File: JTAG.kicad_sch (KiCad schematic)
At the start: 7 parts, among them J2 JTAG_HEADER, J3 JTAG_HEADER

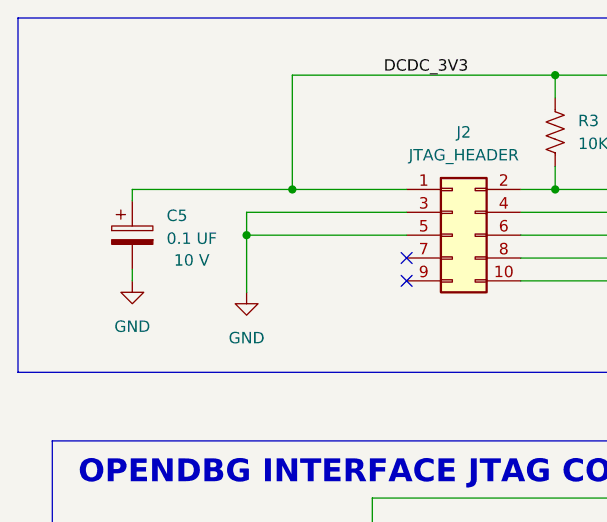
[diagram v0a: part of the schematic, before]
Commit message: menambah lebih dari setengah footprint
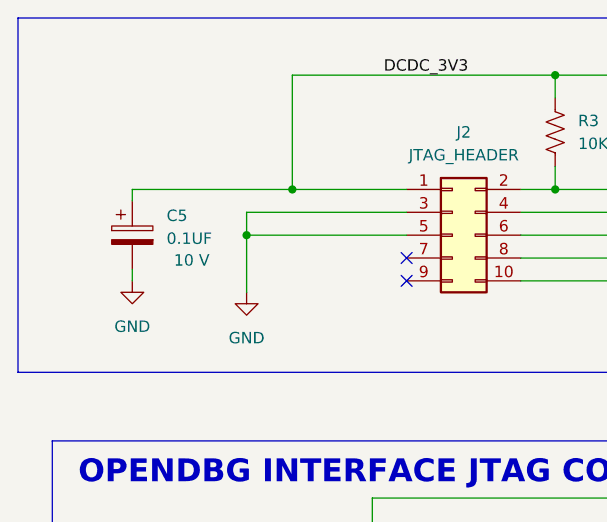
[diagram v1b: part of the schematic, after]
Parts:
- C33: footprint (none) -> Capacitor_SMD:C_0402_1005Metric; MANUFACTURER (none) -> CC0402KRX5R6BB104
- C5: value 0.1 UF -> 0.1UF; footprint (none) -> Capacitor_SMD:C_0402_1005Metric; MANUFACTURER (none) -> CC0402KRX5R6BB104
- R24, R3, R4: footprint (none) -> Resistor_SMD:R_0402_1005Metric
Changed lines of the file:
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@@
 			)
 		)
-		(property "Footprint" ""
+		(property "Footprint" "Resistor_SMD:R_0402_1005Metric"
 			(at 111.506 32.004 90)
 			(effects
@@
 			)
 		)
+		(property "DigikeyPartNumber" ""
+			(at 110.49 31.75 0)
+			(effects
+				(font
+					(size 1.27 1.27)
+				)
+				(hide yes)
+			)
+		)
 		(pin "1"
 		)
@@
 			)
 		)
-		(property "Value" "0.1 UF"
+		(property "Value" "0.1UF"
 			(at 67.31 43.5609 0)
 			(effects
@@
 			)
 		)
-		(property "Footprint" ""
+		(property "Footprint" "Capacitor_SMD:C_0402_1005Metric"
 			(at 64.4652 46.99 0)
 			(effects
@@
 					(size 1.27 1.27)
 				)
+			)
+		)
+		(property "DigikeyPartNumber" ""
+			(at 63.5 43.18 0)
+			(effects
+				(font
+					(size 1.27 1.27)
+				)
+				(hide yes)
+			)
+		)
+		(property "MANUFACTURER" "CC0402KRX5R6BB104"
+			(at 63.5 43.18 0)
+			(effects
+				(font
+					(size 1.27 1.27)
+				)
+				(hide yes)
 			)
 		)
@@
 			)
 		)
+		(property "DigikeyPartNumber" ""
+			(at 99.06 43.18 0)
+			(effects
+				(font
+					(size 1.27 1.27)
+				)
+				(hide yes)
+			)
+		)
 		(pin "8"
 		)
@@
 			)
 		)
-		(property "Footprint" ""
+		(property "Footprint" "Resistor_SMD:R_0402_1005Metric"
 			(at 120.396 32.004 90)
 			(effects
@@
 		)
 		(property "Description" "Resistor, US symbol"
+			(at 119.38 31.75 0)
+			(effects
+				(font
+					(size 1.27 1.27)
+				)
+				(hide yes)
+			)
+		)
+		(property "DigikeyPartNumber" ""
 			(at 119.38 31.75 0)
 			(effects
@@
 			)
 		)
-		(property "Footprint" ""
+		(property "Footprint" "Capacitor_SMD:C_0402_1005Metric"
 			(at 74.93 88.9 0)
 			(effects
@@
 					(size 1.27 1.27)
 				)
+			)
+		)
+		(property "DigikeyPartNumber" ""
+			(at 74.93 88.9 0)
+			(effects
+				(font
+					(size 1.27 1.27)
+				)
+				(hide yes)
+			)
+		)
+		(property "MANUFACTURER" "CC0402KRX5R6BB104"
+			(at 74.93 88.9 0)
+			(effects
+				(font
+					(size 1.27 1.27)
+				)
+				(hide yes)
 			)
 		)
@@
 			)
 		)
+		(property "DigikeyPartNumber" ""
+			(at 107.95 87.63 0)
+			(effects
+				(font
+					(size 1.27 1.27)
+				)
+				(hide yes)
+			)
+		)
 		(pin "8"
 		)
@@
 			)
 		)
-		(property "Footprint" ""
+		(property "Footprint" "Resistor_SMD:R_0402_1005Metric"
 			(at 119.634 77.216 90)
 			(effects
@@
 			(at 120.65 77.47 0)
 			(effects
+				(font
+					(size 1.27 1.27)
+				)
+				(hide yes)
+			)
+		)
+		(property "DigikeyPartNumber" ""
+			(at 120.65 77.47 0)
+			(effects

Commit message: da
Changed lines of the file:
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@@
 		)
 	)
-	(label "JTAG_TCK"
+	(global_label "JTAG_TDI"
+		(shape input)
+		(at 127 45.72 0)
+		(fields_autoplaced yes)
+		(effects
+			(font
+				(size 1.27 1.27)
+			)
+			(justify left)
+		)
+		(property "Intersheetrefs" "${INTERSHEET_REFS}"
+			(at 138.089 45.72 0)
+			(effects
+				(font
+					(size 1.27 1.27)
+				)
+				(justify left)
+				(hide yes)
+			)
+		)
+	)
+	(global_label "P3V3_SDA"
+		(shape input)
+		(at 78.74 82.55 0)
+		(fields_autoplaced yes)
+		(effects
+			(font
+				(size 1.27 1.27)
+			)
+			(justify left)
+		)
+		(property "Intersheetrefs" "${INTERSHEET_REFS}"
+			(at 91.0385 82.55 0)
+			(effects
+				(font
+					(size 1.27 1.27)
+				)
+				(justify left)
+				(hide yes)
+			)
+		)
+	)
+	(global_label "JTAG_TDO"
+		(shape input)
+		(at 127 43.18 0)
+		(fields_autoplaced yes)
+		(effects
+			(font
+				(size 1.27 1.27)
+			)
+			(justify left)
+		)
+		(property "Intersheetrefs" "${INTERSHEET_REFS}"
+			(at 138.8147 43.18 0)
+			(effects
+				(font
+					(size 1.27 1.27)
+				)
+				(justify left)
+				(hide yes)
+			)
+		)
+	)
+	(global_label "JTAG_TRSTB"
+		(shape input)
+		(at 127 48.26 0)
+		(fields_autoplaced yes)
+		(effects
+			(font
+				(size 1.27 1.27)
+			)
+			(justify left)
+		)
+		(property "Intersheetrefs" "${INTERSHEET_REFS}"
+			(at 140.9313 48.26 0)
+			(effects
+				(font
+					(size 1.27 1.27)
+				)
+				(justify left)
+				(hide yes)
+			)
+		)
+	)
+	(global_label "DCDC_3V3"
+		(shape input)
+		(at 91.44 25.4 0)
+		(fields_autoplaced yes)
+		(effects
+			(font
+				(size 1.27 1.27)
+			)
+			(justify left)
+		)
+		(property "Intersheetrefs" "${INTERSHEET_REFS}"
+			(at 103.9804 25.4 0)
+			(effects
+				(font
+					(size 1.27 1.27)
+				)
+				(justify left)
+				(hide yes)
+			)
+		)
+	)
+	(global_label "SDA_JTAG_TDO"
+		(shape input)
+		(at 134.62 87.63 180)
+		(fields_autoplaced yes)
+		(effects
+			(font
+				(size 1.27 1.27)
+			)
+			(justify right)
+		)
+		(property "Intersheetrefs" "${INTERSHEET_REFS}"
+			(at 118.2696 87.63 0)
+			(effects
+				(font
+					(size 1.27 1.27)
+				)
+				(justify right)
+				(hide yes)
+			)
+		)
+	)
+	(global_label "SDA_JTAG_TCLK"
+		(shape input)
+		(at 134.62 85.09 180)
+		(fields_autoplaced yes)
+		(effects
+			(font
+				(size 1.27 1.27)
+			)
+			(justify right)
+		)
+		(property "Intersheetrefs" "${INTERSHEET_REFS}"
+			(at 117.302 85.09 0)
+			(effects
+				(font
+					(size 1.27 1.27)
+				)
+				(justify right)
+				(hide yes)
+			)
+		)
+	)
+	(global_label "SDA_RST"
+		(shape input)
+		(at 134.62 92.71 180)
+		(fields_autoplaced yes)
+		(effects
+			(font
+				(size 1.27 1.27)
+			)
+			(justify right)
+		)
+		(property "Intersheetrefs" "${INTERSHEET_REFS}"
+			(at 123.652 92.71 0)
+			(effects
+				(font
+					(size 1.27 1.27)
+				)
+				(justify right)
+				(hide yes)
+			)
+		)
+	)
+	(global_label "SDA_JTAG_TMS"
+		(shape input)
+		(at 134.62 82.55 180)
+		(fields_autoplaced yes)
+		(effects
+			(font
+				(size 1.27 1.27)
+			)
+			(justify right)
+		)
+		(property "Intersheetrefs" "${INTERSHEET_REFS}"
+			(at 118.2092 82.55 0)
+			(effects
+				(font
+					(size 1.27 1.27)
+				)
+				(justify right)
+				(hide yes)
+			)
+		)
+	)
+	(global_label "JTAG_TCK"
+		(shape input)
 		(at 127 40.64 0)
 		(fields_autoplaced yes)
@@
 				(size 1.27 1.27)
 			)
-			(justify left bottom)
-		)
-	)
-	(label "P3V3_SDA"
-		(at 78.74 82.55 0)
-		(fields_autoplaced yes)
-		(effects
-			(font
-				(size 1.27 1.27)
-			)
-			(justify left bottom)
-		)
-	)
-	(label "DCDC_3V3"
-		(at 91.44 25.4 0)
-		(fields_autoplaced yes)
-		(effects
-			(font
-				(size 1.27 1.27)
-			)
-			(justify left bottom)
-		)
-	)
-	(label "JTAG_TRSTB"
-		(at 127 48.26 0)
-		(fields_autoplaced yes)
-		(effects
-			(font
-				(size 1.27 1.27)
-			)
-			(justify left bottom)
-		)
-	)
-	(label "JTAG_TDO"
-		(at 127 43.18 0)
-		(fields_autoplaced yes)
-		(effects
-			(font
-				(size 1.27 1.27)
-			)
-			(justify left bottom)
-		)
-	)
-	(label "SDA_JTAG_TMS"
-		(at 134.62 82.55 180)
-		(fields_autoplaced yes)
-		(effects
-			(font
-				(size 1.27 1.27)
-			)
-			(justify right bottom)
-		)
-	)
-	(label "JTAG_TDI"
-		(at 127 45.72 0)
-		(fields_autoplaced yes)
-		(effects
-			(font
-				(size 1.27 1.27)
-			)
-			(justify left bottom)
-		)
-	)
-	(label "SDA_JTAG_TDI"
+			(justify left)
+		)
+		(property "Intersheetrefs" "${INTERSHEET_REFS}"
+			(at 138.7542 40.64 0)
+			(effects
+				(font
+					(size 1.27 1.27)
+				)
+				(justify left)
+				(hide yes)
+			)
+		)
+	)
+	(global_label "SDA_JTAG_TDI"
+		(shape input)
 		(at 134.62 90.17 180)
 		(fields_autoplaced yes)
@@
 				(size 1.27 1.27)
 			)
-			(justify right bottom)
-		)
-	)
-	(label "SDA_RST"
-		(at 134.62 92.71 180)
-		(fields_autoplaced yes)
-		(effects
-			(font
-				(size 1.27 1.27)
-			)
-			(justify right bottom)
-		)
-	)
-	(label "SDA_JTAG_TCLK"
-		(at 134.62 85.09 180)
-		(fields_autoplaced yes)
-		(effects
-			(font
-				(size 1.27 1.27)
-			)
-			(justify right bottom)
-		)
-	)
-	(label "SDA_JTAG_TDO"
-		(at 134.62 87.63 180)
-		(fields_autoplaced yes)
-		(effects
-			(font
-				(size 1.27 1.27)
-			)
-			(justify right bottom)
-		)
-	)
-	(label "JTAG_TMS"
+			(justify right)
+		)
+		(property "Intersheetrefs" "${INTERSHEET_REFS}"
+			(at 118.9953 90.17 0)
+			(effects
+				(font
+					(size 1.27 1.27)
+				)
+				(justify right)
+				(hide yes)
+			)
+		)
+	)
+	(global_label "JTAG_TMS"
+		(shape input)
 		(at 127 38.1 0)
 		(fields_autoplaced yes)
@@
 				(size 1.27 1.27)
 			)
-			(justify left bottom)
-		)
-	)
+			(justify left)
+		)
+		(property "Intersheetrefs" "${INTERSHEET_REFS}"
+			(at 138.8751 38.1 0)
+			(effects
+				(font
+					(size 1.27 1.27)
+				)
+				(justify left)
+				(hide yes)
+			)
+		)
+	)

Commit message: add some revision
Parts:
- removed C33: 0.1UF, Capacitor_SMD:C_0402_1005Metric, symbol Device:C_Polarized_US
- removed J3: JTAG_HEADER, symbol Connector_Generic:Conn_02x05_Odd_Even
- added J14, J15, J16, J3: Conn_01x02_Pin, symbol Connector:Conn_01x02_Pin
- added R78, R79, R84, R85: 1k, symbol Device:R_US
- added R80, R81, R82, R83: 4.7k, symbol Device:R_US
- R24: value 10K -> 4.7k; footprint Resistor_SMD:R_0402_1005Metric -> (none)
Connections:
- net P3V3_SDA is gone; now on net GND: R24.2
- net DCDC_3V3: now also R78.1, R79.1, R84.1, R85.1
- net GND: now also R80.2, R81.2, R82.2, R83.2
- net SDA_JTAG_TMS renamed GPIO_SD_02
- net GPIO_SD_02: now also J3.1 (Pin_1)
- new net: J16.2 (Pin_2), R84.2
- new net: J14.2 (Pin_2), R79.2
- new net: J15.2 (Pin_2), R85.2
- new net: J3.2 (Pin_2), R78.2
- new net GPIO_SD_00: R80.1
- new net GPIO_SD_01: J14.1 (Pin_1)
- new net GPIO_SD_03: J15.1 (Pin_1), R83.1
- new net GPIO_SD_04: J16.1 (Pin_1), R82.1
- new net GPIO_SD_13: R81.1
- no-connect marks 4 -> 2
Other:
- note removed: "OPENDBG INTERFACE JTAG CONNECTOR"
